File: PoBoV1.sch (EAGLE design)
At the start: 86 parts, among them IC1 INA232, Q1 IPZ40N04S5L-4R8, Q2 IPZ40N04S5L-4R8, U1 TPS55288RPMR, X1 +Vin, X19 ADDRSEL, X2 BANANAJACKBANANAJACK-BLACK, X3 SDA, X4 SCL, X5 VOUT/EXT, X6 FB SEL, X7 EN SEL, X8 MODE SEL, X9 BANANAJACKBANANAJACK-RED

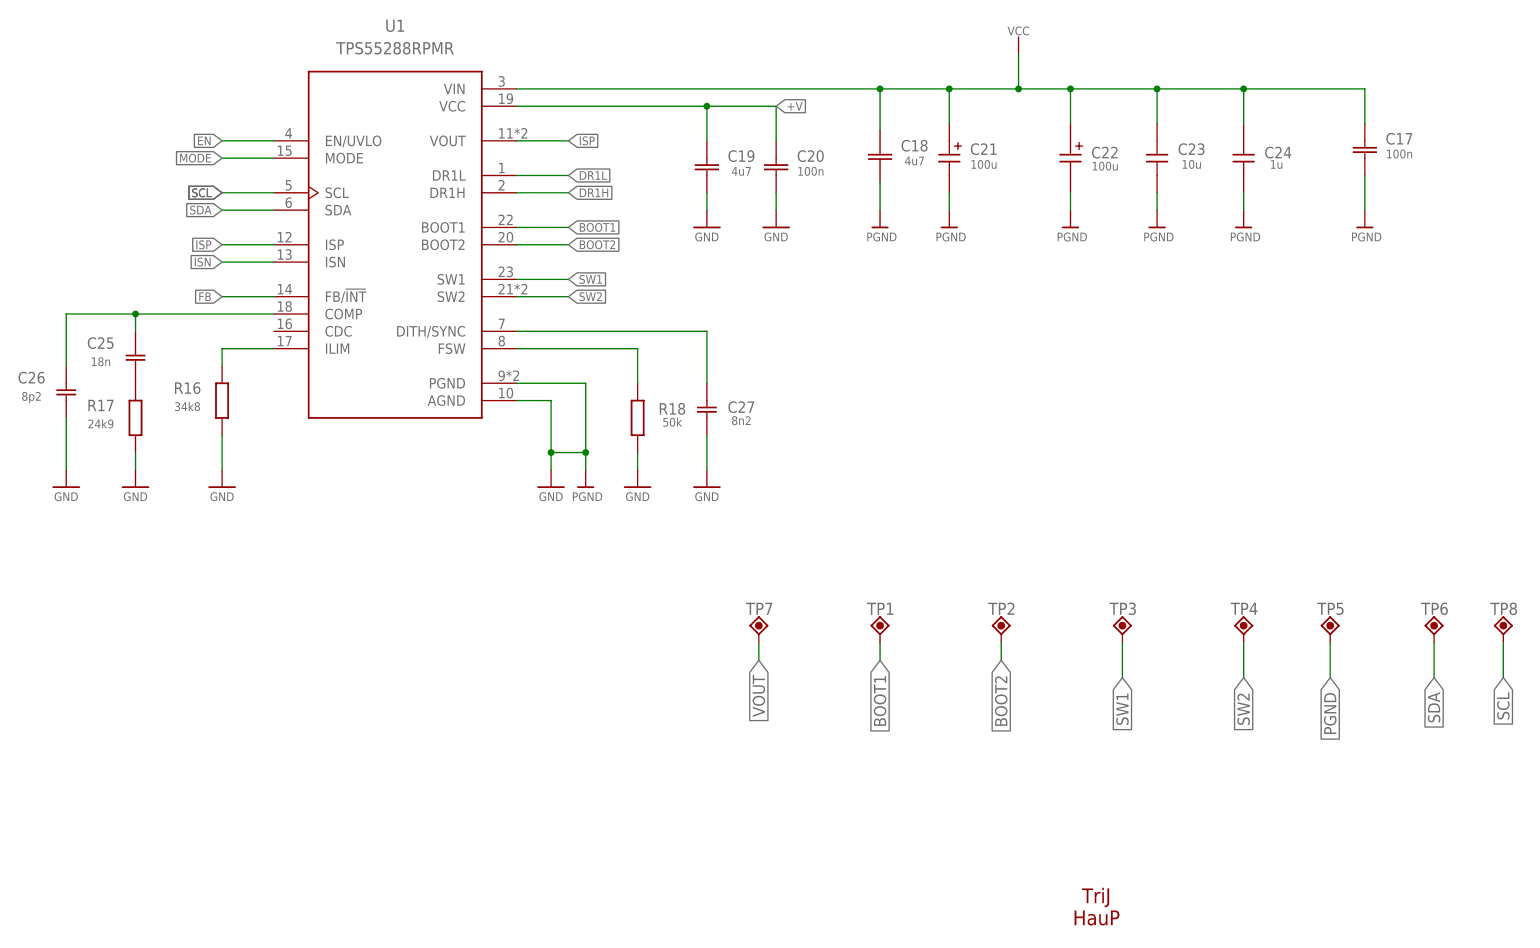
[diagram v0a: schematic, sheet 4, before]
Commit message: Add files via upload
Final Version that includes whole layout revamp
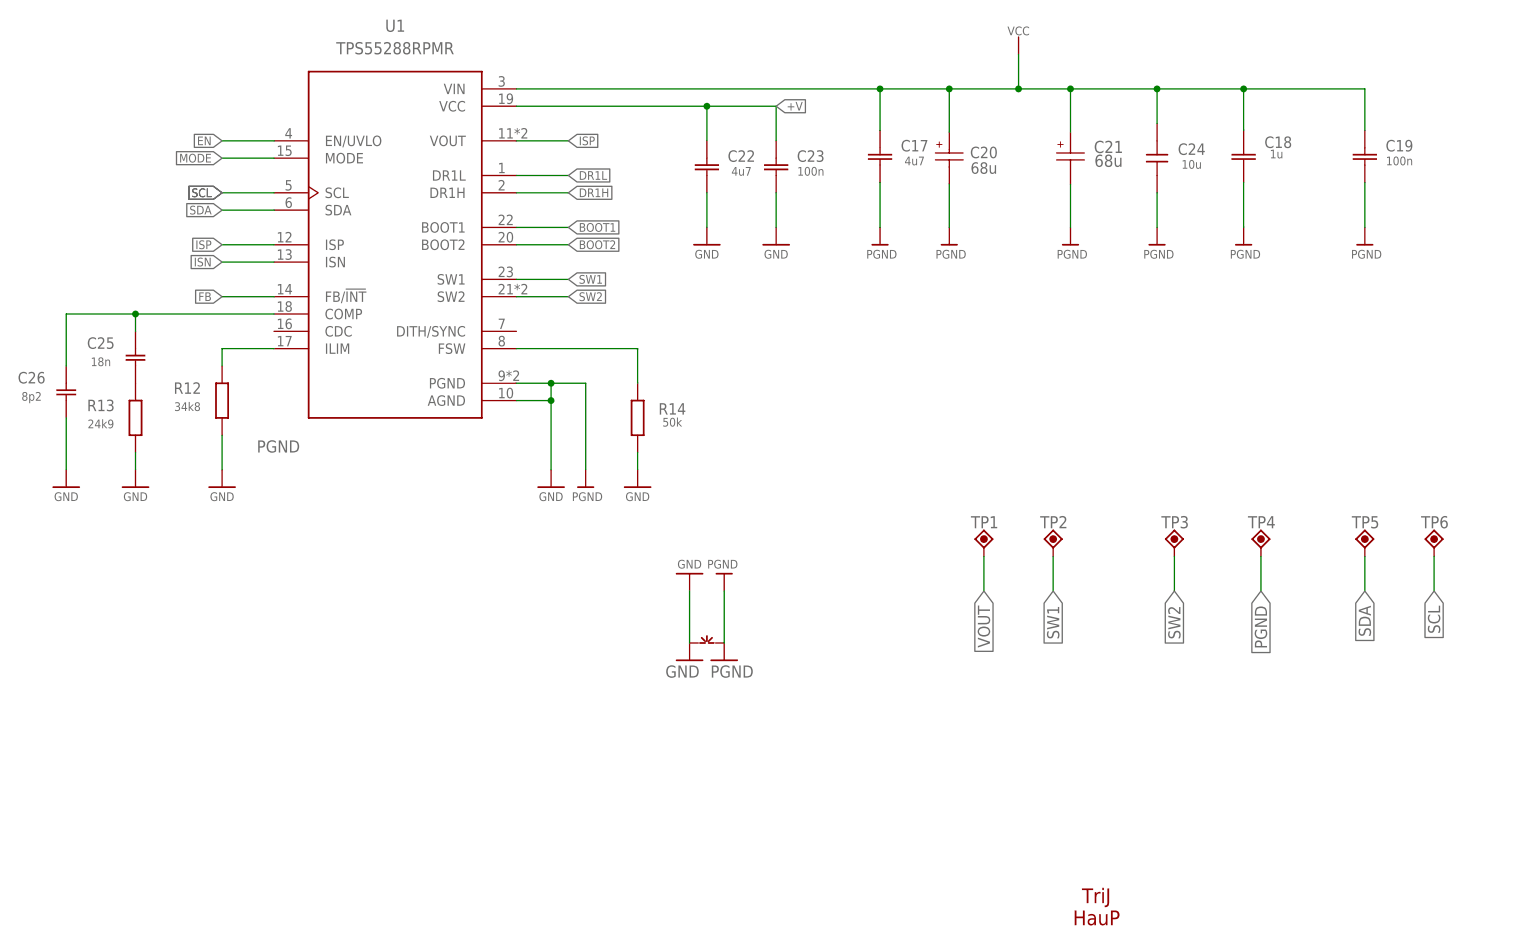
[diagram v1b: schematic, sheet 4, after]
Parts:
- removed C35: 100n, RPoettinger:C-EUC0805
- removed R17: 24k9, RPoettinger:R-EU_R0805
- removed R18: 50k, RPoettinger:R-EU_R0805
- removed R19: 17m, RPoettinger:R-EU_R0805
- removed R20: 5mR, Neo_V2.102R1:RCL_STRH_R-EU_R0805
- removed TP7, TP8: TPP-SMD-20SN, testpoint:TPP-SMD-20SN
- removed X19: ADDRSEL, StefNe555:JUMPER_JP3EJP3E
- removed X9: BANANAJACKBANANAJACK-RED, con_PoeD:BANANAJACKBANANAJACK-RED
- added ~NUDEV~1: GND-GNDA, supply-dummy:GND-GNDA
- C17: value 100n -> 4u7; device RPoettinger:RCL_C-EUC0402 -> RPoettinger:RCL_C-EUC0603
- C18: value 4u7 -> 1u; device RPoettinger:RCL_C-EUC0603 -> RPoettinger:RCL_C-EUC0603K
- C19: value 4u7 -> 100n; device RPoettinger:RCL_C-EUC0603 -> RPoettinger:RCL_C-EUC0402
- C20: value 100n -> 68u; device RPoettinger:RCL_C-EUC0603 -> EEHZA1H680P:EEHZA1H680P
- C21: value 100u -> 68u; device rcl_SekS_V22:C-POL_G -> EEHZA1H680P:EEHZA1H680P
- C22: value 100u -> 4u7; device rcl_SekS_V22:C-POL_G -> RPoettinger:RCL_C-EUC0603
- C23: value 10u -> 100n; device rcl_SekS_V22:C-EU_C1210 -> RPoettinger:RCL_C-EUC0603
- C24: value 1u -> 10u; device rcl_SekS_V22:C-EU_C0402 -> rcl_SekS_V22:C-EU_C1210
- C27: value 8n2 -> 100n
- F1: value 4A -> 7A
- IC1: device FaBo-Sensor:TI-INA219 -> INA232AIDDFR:INA232AIDDFR
- R10: value 115k -> 1R; device rcl_STRH:R-EU_R0805 -> RPoettinger:R-EU_R0805
- R11: value 100k -> 1R; device rcl_STRH:R-EU_R0805 -> RPoettinger:R-EU_R0805
- R12: value 330R -> 34k8; device rcl_STRH:R-EU_R0805 -> RPoettinger:R-EU_R0805
- R13: value 14k3 -> 24k9; device rcl_STRH:R-EU_R0805 -> RPoettinger:R-EU_R0805
- R14: value 1R -> 50k
- R15: value 1R -> 17m
- R16: value 34k8 -> 5mR; device RPoettinger:R-EU_R0805 -> Neo_V2.102R1:RCL_STRH_R-EU_R0805
- R6: value 50R -> 147k
- R7: value 100k -> 115k
- R8: value 11.3k -> 330R
- R9: value 147k -> 14k3
- V1: value SM4001 -> B560C-13-F; device diode_STRH:DIODESOD87 -> B560C-13-F:B560C-13-F
- X2: value BANANAJACKBANANAJACK-BLACK -> SDA; device con_PoeD:BANANAJACKBANANAJACK-BLACK -> RPoettinger:JUMPER_JP3EJP3E
- X3: value SDA -> SCL
- X4: value SCL -> EN SEL
- X5: value VOUT/EXT -> MODE SEL; device Neo_V2.102R1:JUMPER_STRH_JP1E -> RPoettinger:JUMPER_JP3EJP3E
- X6: value FB SEL -> RED; device RPoettinger:JUMPER_JP3EJP3E -> con_PoeD:BANANAJACKBANANAJACK-RED
- X7: value EN SEL -> BLACK; device RPoettinger:JUMPER_JP3EJP3E -> con_PoeD:BANANAJACKBANANAJACK-BLACK
- X8: value MODE SEL -> ADDRSEL; device RPoettinger:JUMPER_JP3EJP3E -> StefNe555:JUMPER_JP3EJP3E
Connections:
- removed net GND: A1.GND, A1.GND@1, A1.GND@2, C14.2, C19.2, C20.2, C26.2, C27.2, C35.2, IC1.GND, R10.1, R13.1, R16.1, R17.1, R18.2, R8.1, U1.AGND, U1.PGND, X19.1, X3.1, X4.1, X7.1, X8.3
- removed net N$11: R7.2, X5.2
- removed net N$16: R6.1, X5.1
- removed net N$22: F1.2, V1.A
- removed net N$4: R11.2, X6.3
- removed net N$6: C27.1, U1.DITH/SYNC
- removed net N$8: R7.1, R8.2, X6.1
- net +3.3: now also C27.1, IC1.VS
- net +3.3V: now also X8.3; no longer C35.1, IC1.VS, X19.3
- net +5V: now also R6.2, R8.2; no longer R12.2, R9.2
- net +V: now also C22.1, C23.1; no longer C19.1, C20.1, R11.1
- net ADDRSEL: now also X8.2; no longer X19.2
- net BOOT1: no longer TP1.P
- net BOOT2: no longer TP2.P
- net DR1H: now also R10.1; no longer R14.1
- net DR1L: now also R11.1; no longer R15.1
- net EN: now also X4.2; no longer X7.2
- net FB: no longer X6.2
- net ISN: now also R15.1, R16.2; no longer R19.1, R20.2
- net ISP: now also R15.2; no longer R19.2
- net MODE: now also X5.2; no longer X8.2
- net N$10: now also X3.3; no longer X4.3
- net N$12: now also R13.2; no longer R17.2
- net N$14: now also R14.1; no longer R18.1
- net N$15: now also R12.2; no longer R16.2
- net N$17: now also R8.1; no longer R12.1
- net N$18: now also R9.2, X5.1; no longer R13.2, X8.1
- net N$20: now also F1.2
- net N$3: now also R10.2; no longer R14.2
- net N$5: now also R11.2; no longer R15.2
- net N$7: now also R6.1, R7.2, X4.3; no longer R10.2, R9.1, X7.3
- net N$9: now also X2.3; no longer X3.3
- net PGND: now also A1.GND, A1.GND@1, A1.GND@2, C14.2, C19.2, C20.2, C21.2, C22.2, C26.2, C27.2, IC1.GND, R12.1, R13.1, R14.2, R7.1, R9.1, TP4.P, U1.AGND, U1.PGND, V1.A, X2.1, X3.1, X4.1, X5.3, X7.2, X8.1, ~NUDEV~1.GND, ~NUDEV~1.GNDA; no longer C21.-, C22.-, TP5.P, X2.2
- net SCL: now also TP6.P, X3.2; no longer TP8.P, X4.2
- net SDA: now also A1.GPIO22, TP5.P, X2.2; no longer A1.GPIO19, TP6.P, X3.2
- net SW1: now also TP2.P; no longer TP3.P
- net SW2: now also TP3.P; no longer TP4.P
- net VCC: now also C19.1, C20.1, C21.1; no longer C21.+, C22.+, C23.1, R6.2
- net VOUT: now also R16.1, TP1.P, X6.2; no longer R20.1, TP7.P, X9.2
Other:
- note removed: "1: HIGH-Z / INT FB 3: MAX 12V@MAX_REF / EXT FB"
- moved on the sheet: C17, C18, C19, C21, C23, C24, R4, R5, R6, R7, R8, R9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
